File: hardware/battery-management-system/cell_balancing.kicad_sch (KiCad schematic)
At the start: 44 parts, among them IC1 LT8584EFE#PBF, IC2 LT8584EFE#PBF, IC3 LT8584EFE#PBF, IC4 LT8584EFE#PBF, T1 NA6252-ALD, T2 NA6252-ALD, T3 NA6252-ALD, T4 NA6252-ALD

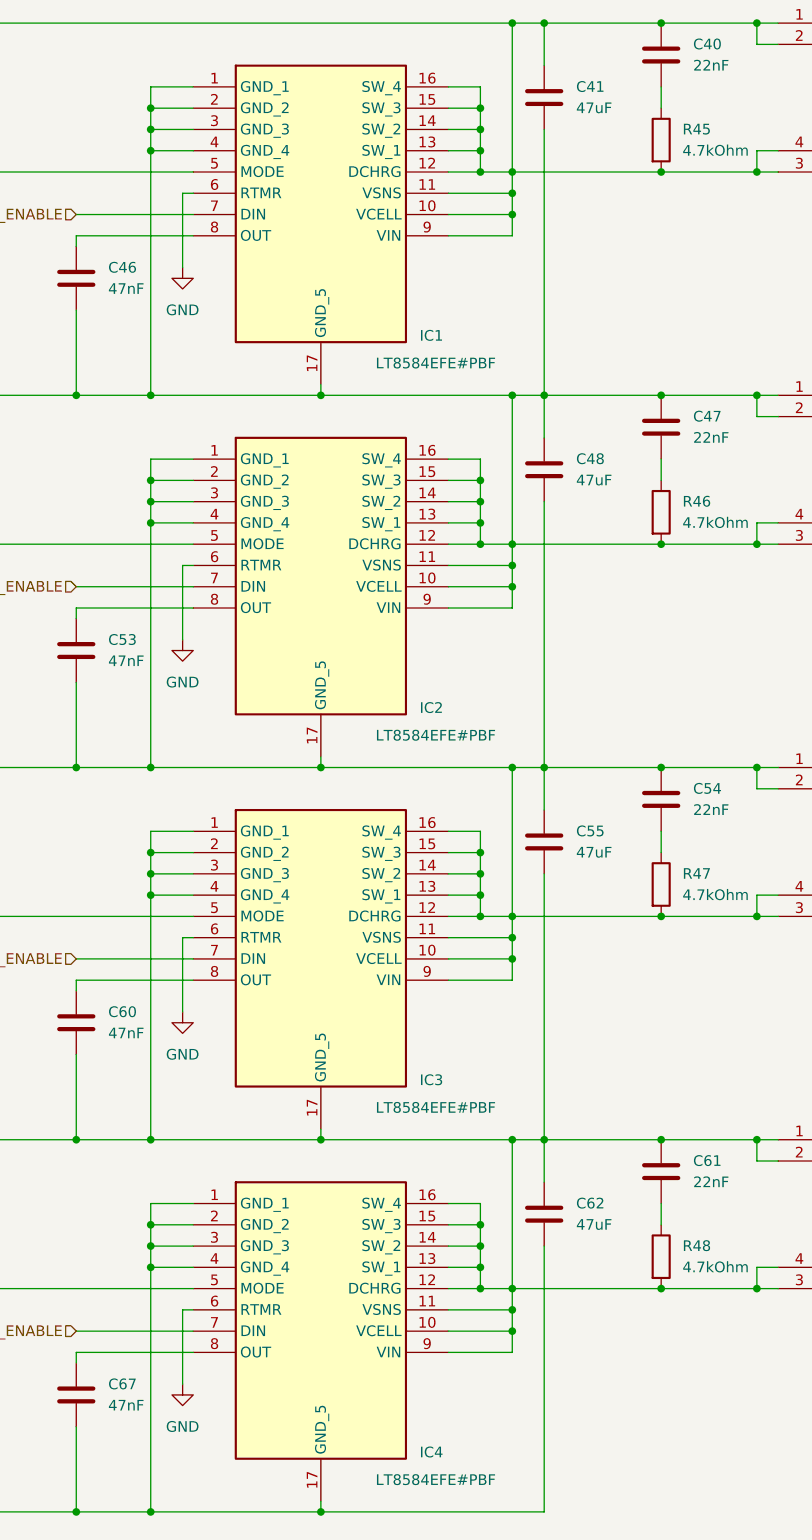
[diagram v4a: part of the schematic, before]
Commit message: finish placement of BMS R03
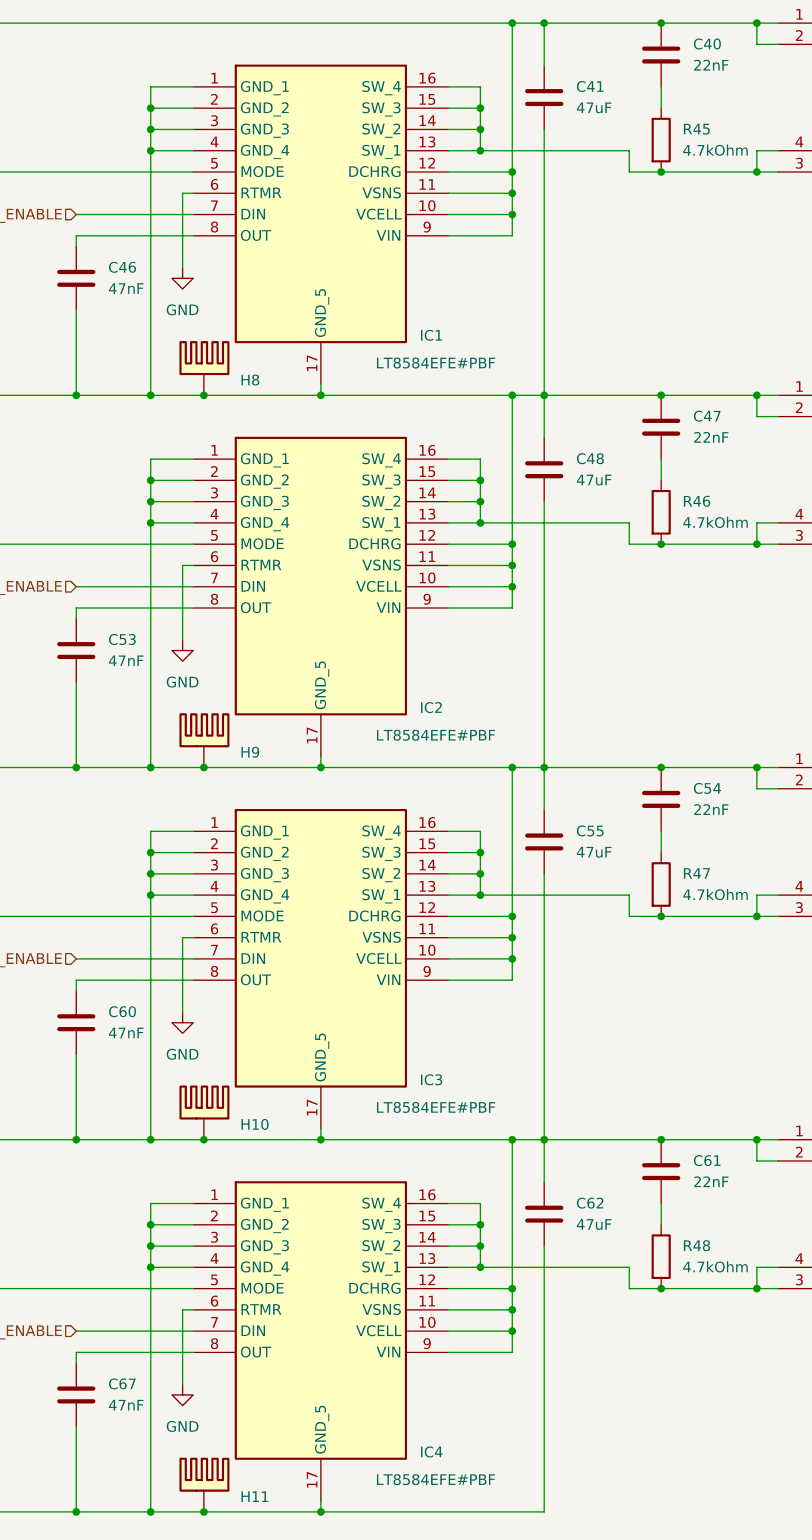
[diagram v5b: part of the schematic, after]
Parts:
- added H10, H11, H8, H9: heatsink_18x18, benediktibk:heatsink_18x18, symbol benediktibk:heatsink_18x18
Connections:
- net CELL1_MINUS: now also H11.PAD
- net CELL2_MINUS: now also H10.PAD; no longer IC4.13 (SW_1), IC4.14 (SW_2), IC4.15 (SW_3), IC4.16 (SW_4), R48.2, T4.3, T4.4
- net CELL3_MINUS: now also H9.PAD; no longer IC3.13 (SW_1), IC3.14 (SW_2), IC3.15 (SW_3), IC3.16 (SW_4), R47.2, T3.3, T3.4
- net CELL4_MINUS: now also H8.PAD; no longer IC2.13 (SW_1), IC2.14 (SW_2), IC2.15 (SW_3), IC2.16 (SW_4), R46.2, T2.3, T2.4
- net PACK: no longer IC1.13 (SW_1), IC1.14 (SW_2), IC1.15 (SW_3), IC1.16 (SW_4), R45.2, T1.3, T1.4
- new net: IC1.13 (SW_1), IC1.14 (SW_2), IC1.15 (SW_3), IC1.16 (SW_4), R45.2, T1.3, T1.4
- new net: IC2.13 (SW_1), IC2.14 (SW_2), IC2.15 (SW_3), IC2.16 (SW_4), R46.2, T2.3, T2.4
- new net: IC4.13 (SW_1), IC4.14 (SW_2), IC4.15 (SW_3), IC4.16 (SW_4), R48.2, T4.3, T4.4
- new net: IC3.13 (SW_1), IC3.14 (SW_2), IC3.15 (SW_3), IC3.16 (SW_4), R47.2, T3.3, T3.4

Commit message: update symbols from library
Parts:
- H10, H11, H8, H9: Mouser Part Number (none) -> 490-HSB06-181810
- IC1, IC2, IC3, IC4: Mouser Part Number (none) -> 584-LT8584EFE#PBF
- T1, T2, T3, T4: Mouser Part Number (none) -> 994-NA6252-ALD
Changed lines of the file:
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@@
 			)
 		)
+		(property "Mouser Part Number" "584-LT8584EFE#PBF"
+			(at 113.03 519.05 0)
+			(effects
+				(font
+					(size 1.27 1.27)
+				)
+				(justify left top)
+				(hide yes)
+			)
+		)
 		(pin "13"
 		)
@@
 			)
 		)
+		(property "Mouser Part Number" "490-HSB06-181810"
+			(at 88.138 51.308 0)
+			(effects
+				(font
+					(size 1.27 1.27)
+				)
+				(hide yes)
+			)
+		)
 		(pin "PAD"
 		)
@@
 			)
 		)
+		(property "Mouser Part Number" "994-NA6252-ALD"
+			(at 172.72 511.43 0)
+			(effects
+				(font
+					(size 1.27 1.27)
+				)
+				(justify left top)
+				(hide yes)
+			)
+		)
 		(pin "4"
 		)
@@
 			)
 		)
+		(property "Mouser Part Number" "994-NA6252-ALD"
+			(at 172.72 555.88 0)
+			(effects
+				(font
+					(size 1.27 1.27)
+				)
+				(justify left top)
+				(hide yes)
+			)
+		)
 		(pin "4"
 		)
@@
 			)
 		)
+		(property "Mouser Part Number" "490-HSB06-181810"
+			(at 88.138 95.758 0)
+			(effects
+				(font
+					(size 1.27 1.27)
+				)
+				(hide yes)
+			)
+		)
 		(pin "PAD"
 		)
@@
 			)
 		)
+		(property "Mouser Part Number" "994-NA6252-ALD"
+			(at 172.72 600.33 0)
+			(effects
+				(font
+					(size 1.27 1.27)
+				)
+				(justify left top)
+				(hide yes)
+			)
+		)
 		(pin "4"
 		)
@@
 			)
 		)
+		(property "Mouser Part Number" "584-LT8584EFE#PBF"
+			(at 113.03 563.5 0)
+			(effects
+				(font
+					(size 1.27 1.27)
+				)
+				(justify left top)
+				(hide yes)
+			)
+		)
 		(pin "13"
 		)
@@
 			)
 		)
+		(property "Mouser Part Number" "994-NA6252-ALD"
+			(at 172.72 644.78 0)
+			(effects
+				(font
+					(size 1.27 1.27)
+				)
+				(justify left top)
+				(hide yes)
+			)
+		)
 		(pin "4"
 		)
@@
 			)
 		)
+		(property "Mouser Part Number" "584-LT8584EFE#PBF"
+			(at 113.03 652.4 0)
+			(effects
+				(font
+					(size 1.27 1.27)
+				)
+				(justify left top)
+				(hide yes)
+			)
+		)
 		(pin "13"
 		)
@@
 			)
 		)
+		(property "Mouser Part Number" "490-HSB06-181810"
+			(at 88.138 184.658 0)
+			(effects
+				(font
+					(size 1.27 1.27)
+				)
+				(hide yes)
+			)
+		)
 		(pin "PAD"
 		)
@@
 			)
 		)
+		(property "Mouser Part Number" "584-LT8584EFE#PBF"
+			(at 113.03 607.95 0)
+			(effects
+				(font
+					(size 1.27 1.27)
+				)
+				(justify left top)
+				(hide yes)
+			)
+		)
 		(pin "13"
 		)
@@
 			(at 88.138 140.208 0)
 			(effects
+				(font
+					(size 1.27 1.27)
+				)
+				(hide yes)
+			)
+		)
+		(property "Mouser Part Number" "490-HSB06-181810"
+			(at 88.138 140.208 0)
+			(effects

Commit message: update symbols from library
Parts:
- C41, C45, C48, C52, C55, C59, C62, C66: Mouser Part Number (none) -> 810-C3216X5R1E476M
- C42, C49, C56, C63: Mouser Part Number (none) -> 963-UMK107BJ105KA-T
- C43, C44, C50, C51, C57, C58, C64, C65: Mouser Part Number (none) -> 187-CL31A106MBHNNNE
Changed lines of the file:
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@@
 			)
 		)
+		(property "Mouser Part Number" "187-CL31A106MBHNNNE"
+			(at 232.156 157.48 0)
+			(effects
+				(font
+					(size 1.27 1.27)
+				)
+				(hide yes)
+			)
+		)
 		(pin "1"
 		)
@@
 			)
 		)
+		(property "Mouser Part Number" "187-CL31A106MBHNNNE"
+			(at 219.456 113.03 0)
+			(effects
+				(font
+					(size 1.27 1.27)
+				)
+				(hide yes)
+			)
+		)
 		(pin "1"
 		)
@@
 			)
 		)
+		(property "Mouser Part Number" "187-CL31A106MBHNNNE"
+			(at 232.156 24.13 0)
+			(effects
+				(font
+					(size 1.27 1.27)
+				)
+				(hide yes)
+			)
+		)
 		(pin "1"
 		)
@@
 			)
 		)
+		(property "Mouser Part Number" "810-C3216X5R1E476M"
+			(at 145.796 113.03 0)
+			(effects
+				(font
+					(size 1.27 1.27)
+				)
+				(hide yes)
+			)
+		)
 		(pin "1"
 		)
@@
 			)
 		)
+		(property "Mouser Part Number" "963-UMK107BJ105KA-T"
+			(at 206.756 113.03 0)
+			(effects
+				(font
+					(size 1.27 1.27)
+				)
+				(hide yes)
+			)
+		)
 		(pin "1"
 		)
@@
 			)
 		)
+		(property "Mouser Part Number" "187-CL31A106MBHNNNE"
+			(at 232.156 68.58 0)
+			(effects
+				(font
+					(size 1.27 1.27)
+				)
+				(hide yes)
+			)
+		)
 		(pin "1"
 		)
@@
 			)
 		)
+		(property "Mouser Part Number" "810-C3216X5R1E476M"
+			(at 48.006 171.45 0)
+			(effects
+				(font
+					(size 1.27 1.27)
+				)
+				(hide yes)
+			)
+		)
 		(pin "1"
 		)
@@
 			)
 		)
+		(property "Mouser Part Number" "810-C3216X5R1E476M"
+			(at 145.796 157.48 0)
+			(effects
+				(font
+					(size 1.27 1.27)
+				)
+				(hide yes)
+			)
+		)
 		(pin "1"
 		)
@@
 			)
 		)
+		(property "Mouser Part Number" "187-CL31A106MBHNNNE"
+			(at 219.456 157.48 0)
+			(effects
+				(font
+					(size 1.27 1.27)
+				)
+				(hide yes)
+			)
+		)
 		(pin "1"
 		)
@@
 			)
 		)
+		(property "Mouser Part Number" "810-C3216X5R1E476M"
+			(at 48.006 82.55 0)
+			(effects
+				(font
+					(size 1.27 1.27)
+				)
+				(hide yes)
+			)
+		)
 		(pin "1"
 		)
@@
 			)
 		)
+		(property "Mouser Part Number" "187-CL31A106MBHNNNE"
+			(at 232.156 113.03 0)
+			(effects
+				(font
+					(size 1.27 1.27)
+				)
+				(hide yes)
+			)
+		)
 		(pin "1"
 		)
@@
 			)
 		)
+		(property "Mouser Part Number" "810-C3216X5R1E476M"
+			(at 48.006 127 0)
+			(effects
+				(font
+					(size 1.27 1.27)
+				)
+				(hide yes)
+			)
+		)
 		(pin "1"
 		)
@@
 			)
 		)
+		(property "Mouser Part Number" "963-UMK107BJ105KA-T"
+			(at 206.756 157.48 0)
+			(effects
+				(font
+					(size 1.27 1.27)
+				)
+				(hide yes)
+			)
+		)
 		(pin "1"
 		)
@@
 			)
 		)
+		(property "Mouser Part Number" "810-C3216X5R1E476M"
+			(at 48.006 38.1 0)
+			(effects
+				(font
+					(size 1.27 1.27)
+				)
+				(hide yes)
+			)
+		)
 		(pin "1"
 		)
@@
 			)
 		)
+		(property "Mouser Part Number" "963-UMK107BJ105KA-T"
+			(at 206.756 68.58 0)
+			(effects
+				(font
+					(size 1.27 1.27)
+				)
+				(hide yes)
+			)
+		)
 		(pin "1"
 		)
@@
 			)
 		)
+		(property "Mouser Part Number" "187-CL31A106MBHNNNE"
+			(at 219.456 24.13 0)
+			(effects
+				(font
+					(size 1.27 1.27)
+				)
+				(hide yes)
+			)
+		)
 		(pin "1"
 		)
@@
 			)
 		)
+		(property "Mouser Part Number" "810-C3216X5R1E476M"
+			(at 145.796 24.13 0)
+			(effects
+				(font
+					(size 1.27 1.27)
+				)
+				(hide yes)
+			)
+		)
 		(pin "1"
 		)
@@
 			)
 		)
+		(property "Mouser Part Number" "963-UMK107BJ105KA-T"
+			(at 206.756 24.13 0)
+			(effects
+				(font
+					(size 1.27 1.27)
+				)
+				(hide yes)
+			)
+		)
 		(pin "1"
 		)
@@
 			)
 		)
+		(property "Mouser Part Number" "810-C3216X5R1E476M"
+			(at 145.796 68.58 0)
+			(effects
+				(font
+					(size 1.27 1.27)
+				)
+				(hide yes)
+			)
+		)
 		(pin "1"
 		)
@@
 			(at 219.456 68.58 0)
 			(effects
+				(font
+					(size 1.27 1.27)
+				)
+				(hide yes)
+			)
+		)
+		(property "Mouser Part Number" "187-CL31A106MBHNNNE"
+			(at 219.456 68.58 0)
+			(effects
